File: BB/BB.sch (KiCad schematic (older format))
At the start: 37 parts, among them SW0 SW_Push, U1 AT90USB1286-AU, Y0 16Mhz

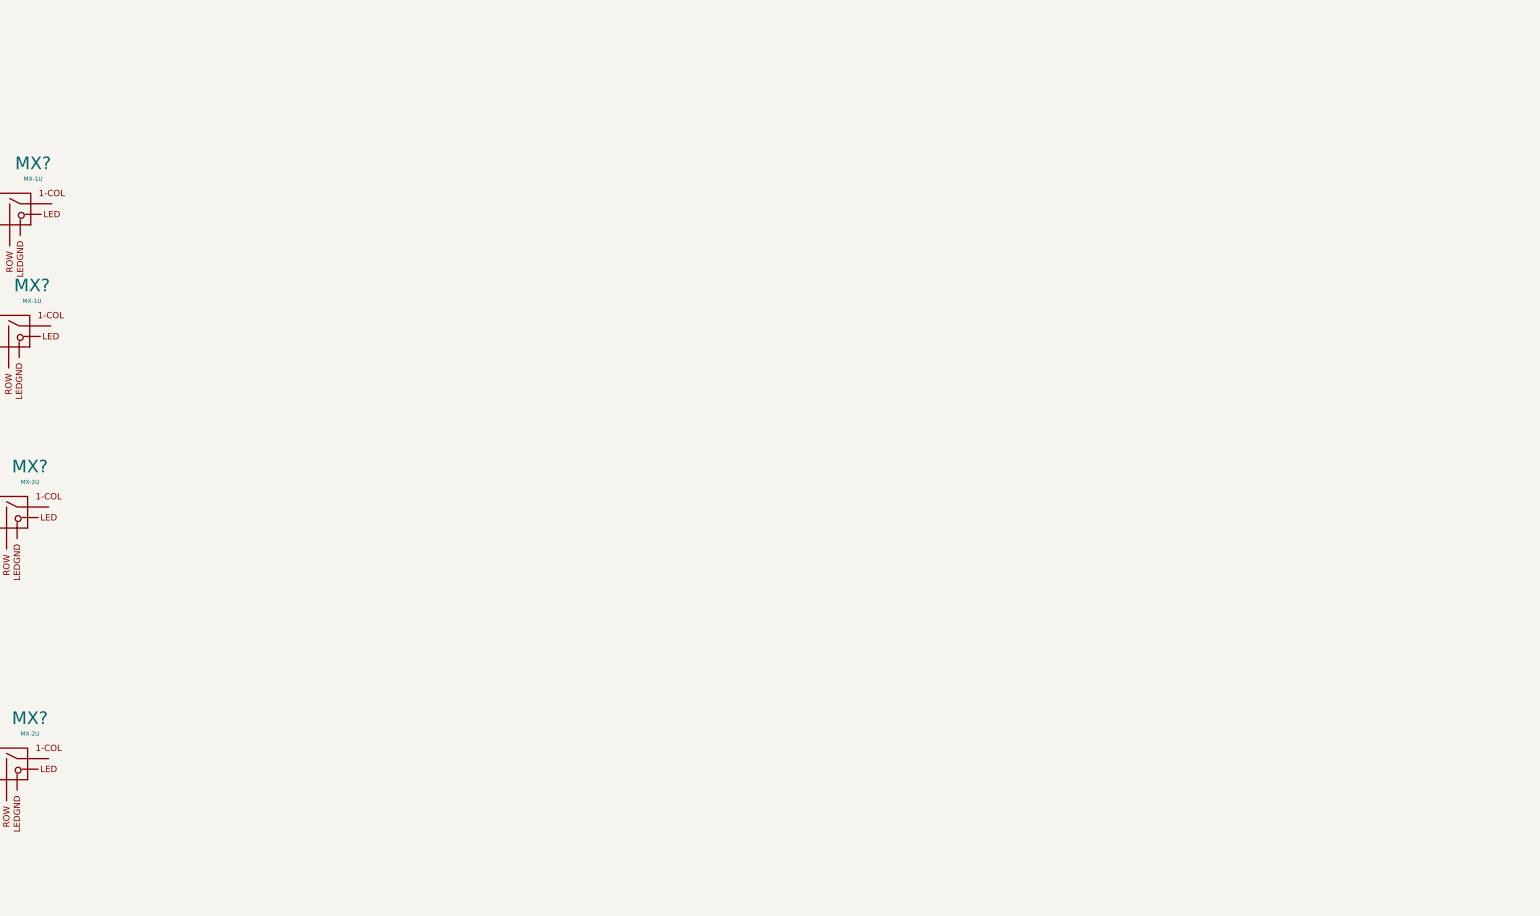
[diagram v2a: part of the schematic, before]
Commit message: All Switches In Place
No diodes yet, waiting for 2-1 diode schematic
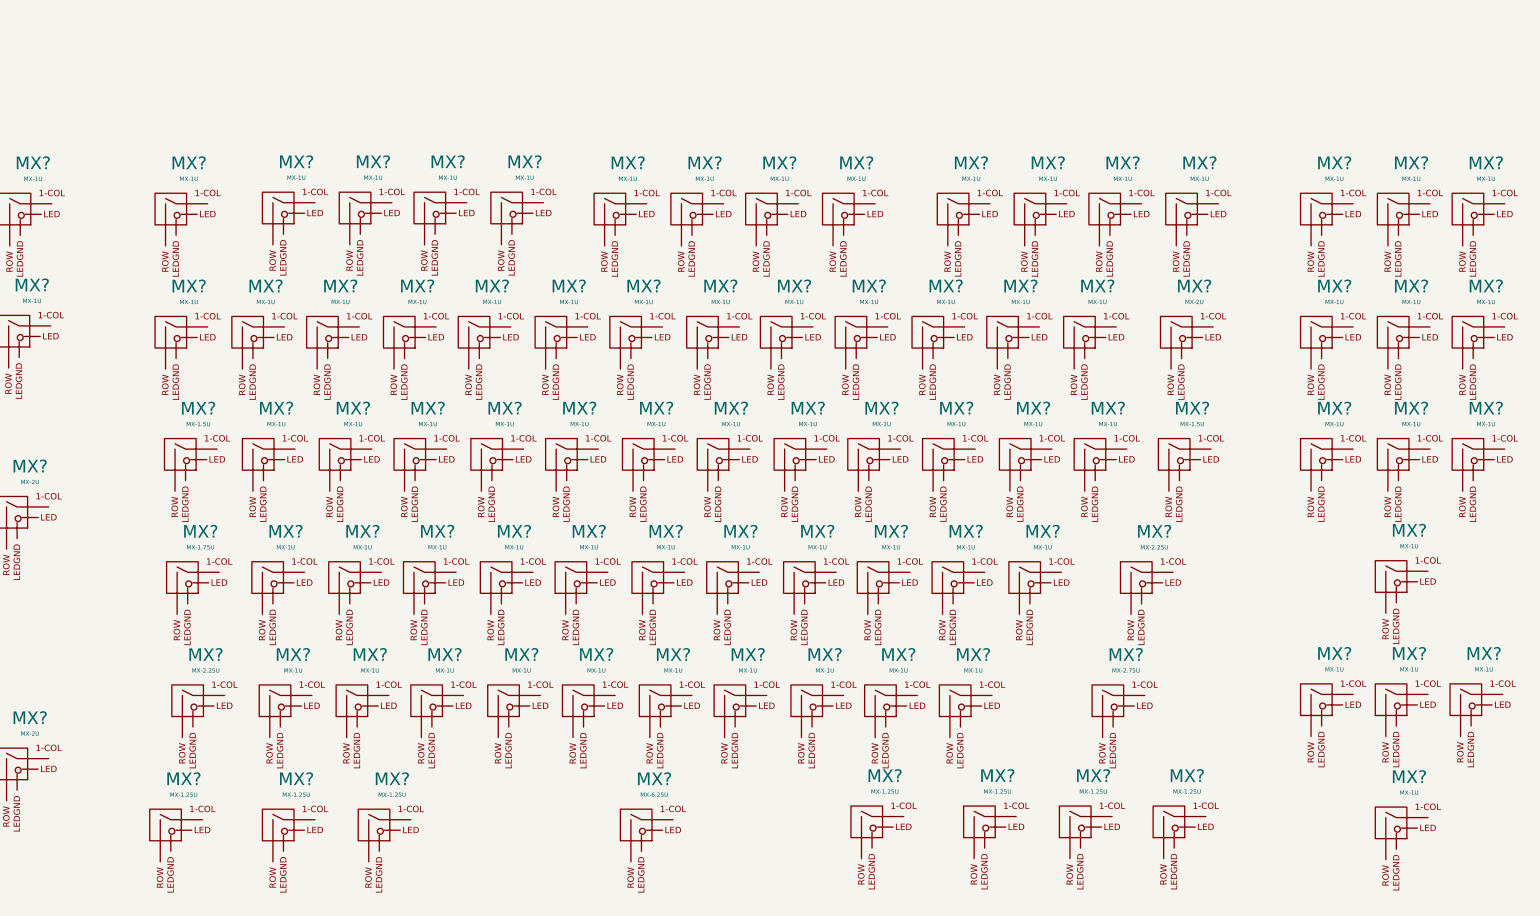
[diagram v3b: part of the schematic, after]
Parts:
- added MX? (x73): MX-1U, symbol MX_Alps_Hybrids:MX-1U
- added MX?: MX-2U, symbol MX_Alps_Hybrids:MX-2U
- added MX? (x2): MX-1.5U, symbol MX_Alps_Hybrids:MX-1.5U
- added MX? (x2): MX-2.25U, symbol MX_Alps_Hybrids:MX-2.25U
- added MX?: MX-1.75U, symbol MX_Alps_Hybrids:MX-1.75U
- added MX?: MX-2.75U, symbol MX_Alps_Hybrids:MX-2.75U
- added MX? (x7): MX-1.25U, symbol MX_Alps_Hybrids:MX-1.25U
- added MX?: MX-6.25U, symbol MX_Alps_Hybrids:MX-6.25U

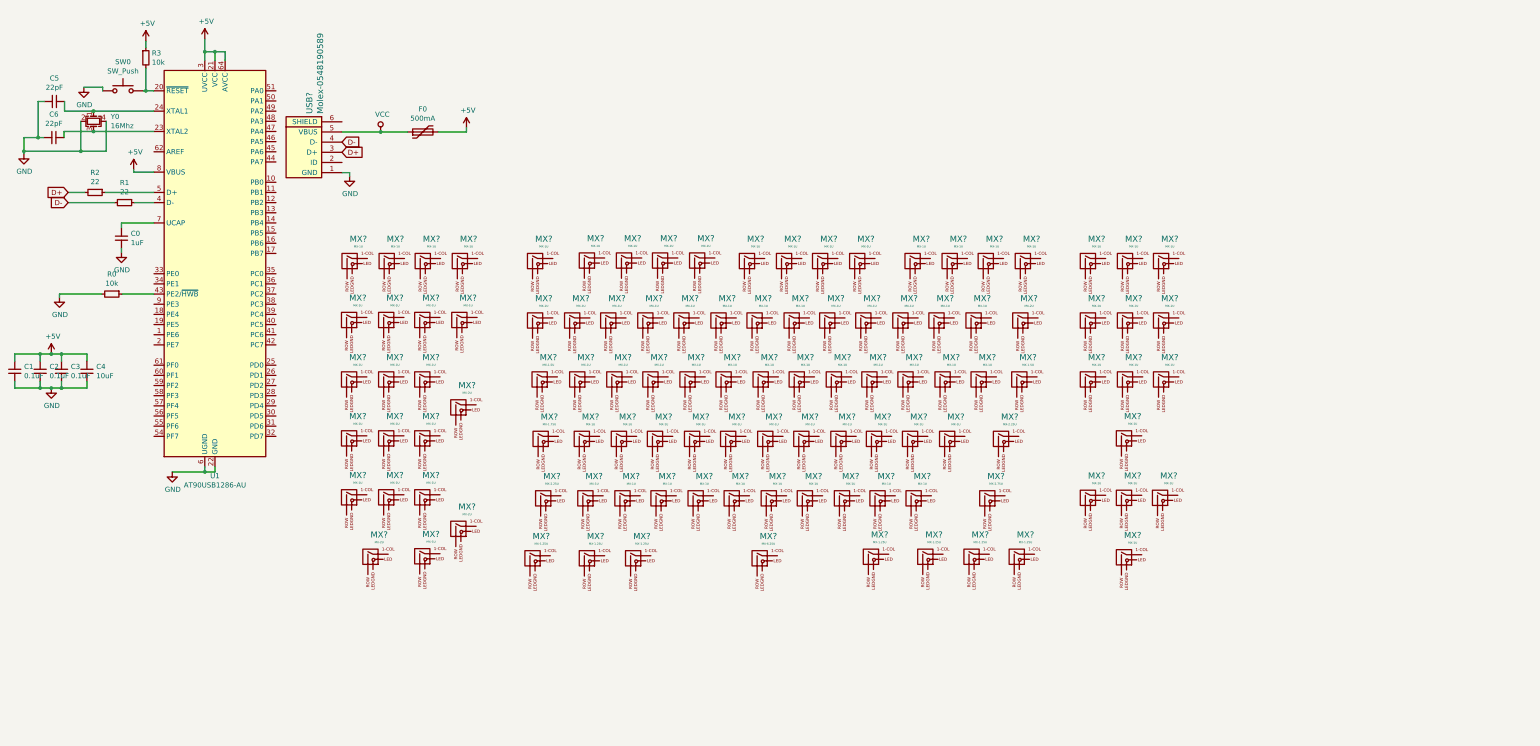
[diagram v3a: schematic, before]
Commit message: Add submodules
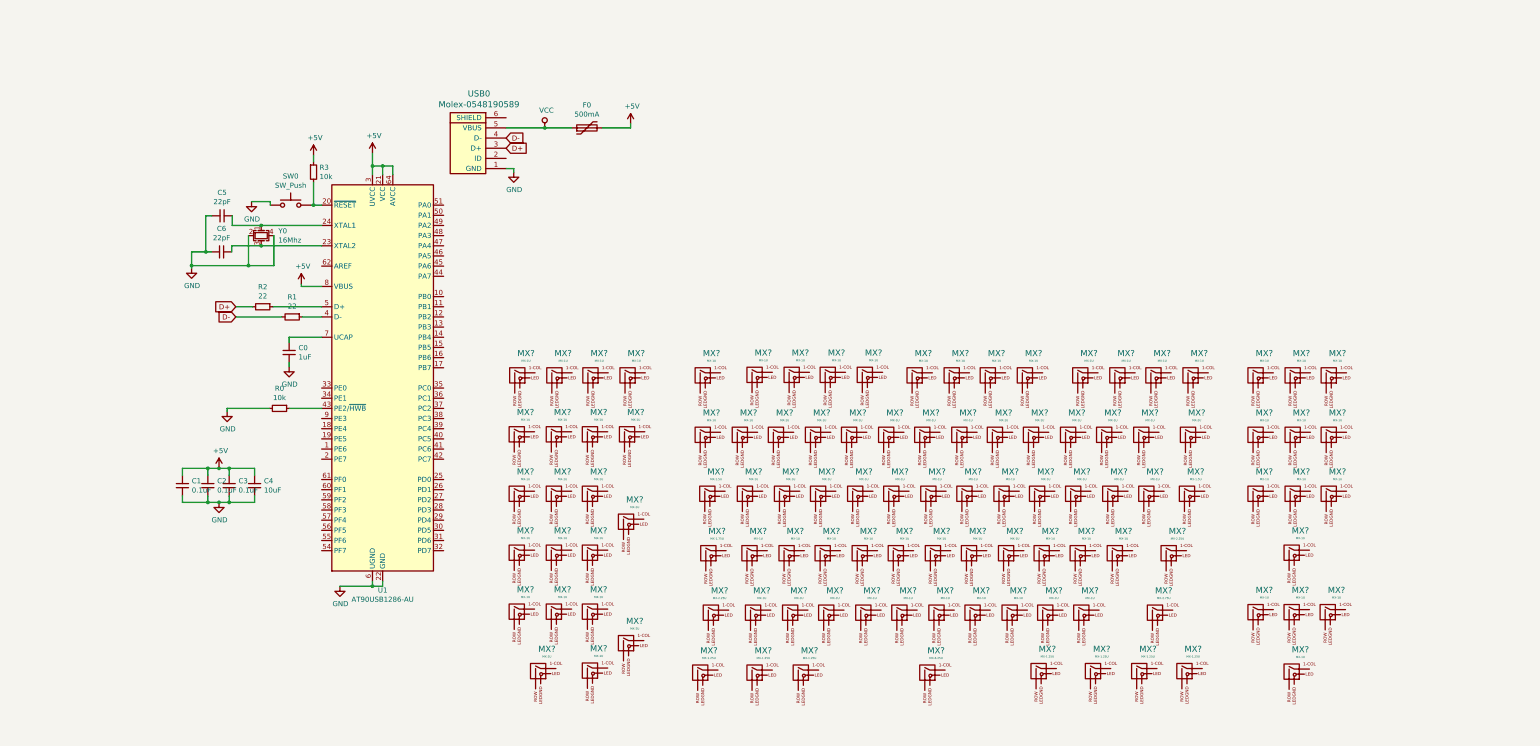
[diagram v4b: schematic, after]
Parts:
- gave numbers to parts that had none: 1
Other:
- moved on the sheet: C0, C1, C2, C3, C4, C5, C6, F0, MX?, R0, R1, R2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

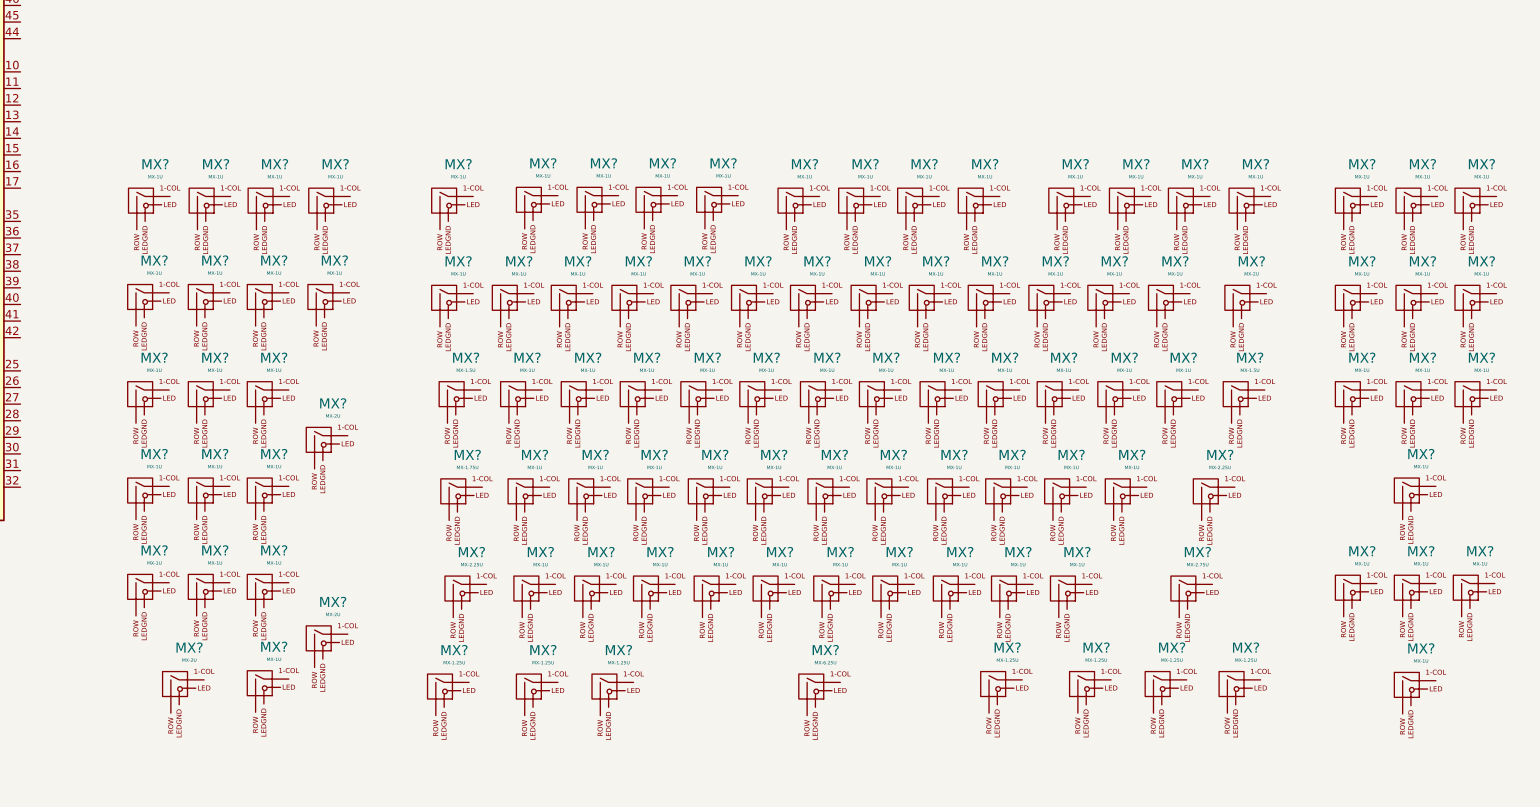
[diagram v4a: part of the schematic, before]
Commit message: All Switches in place with Diodes
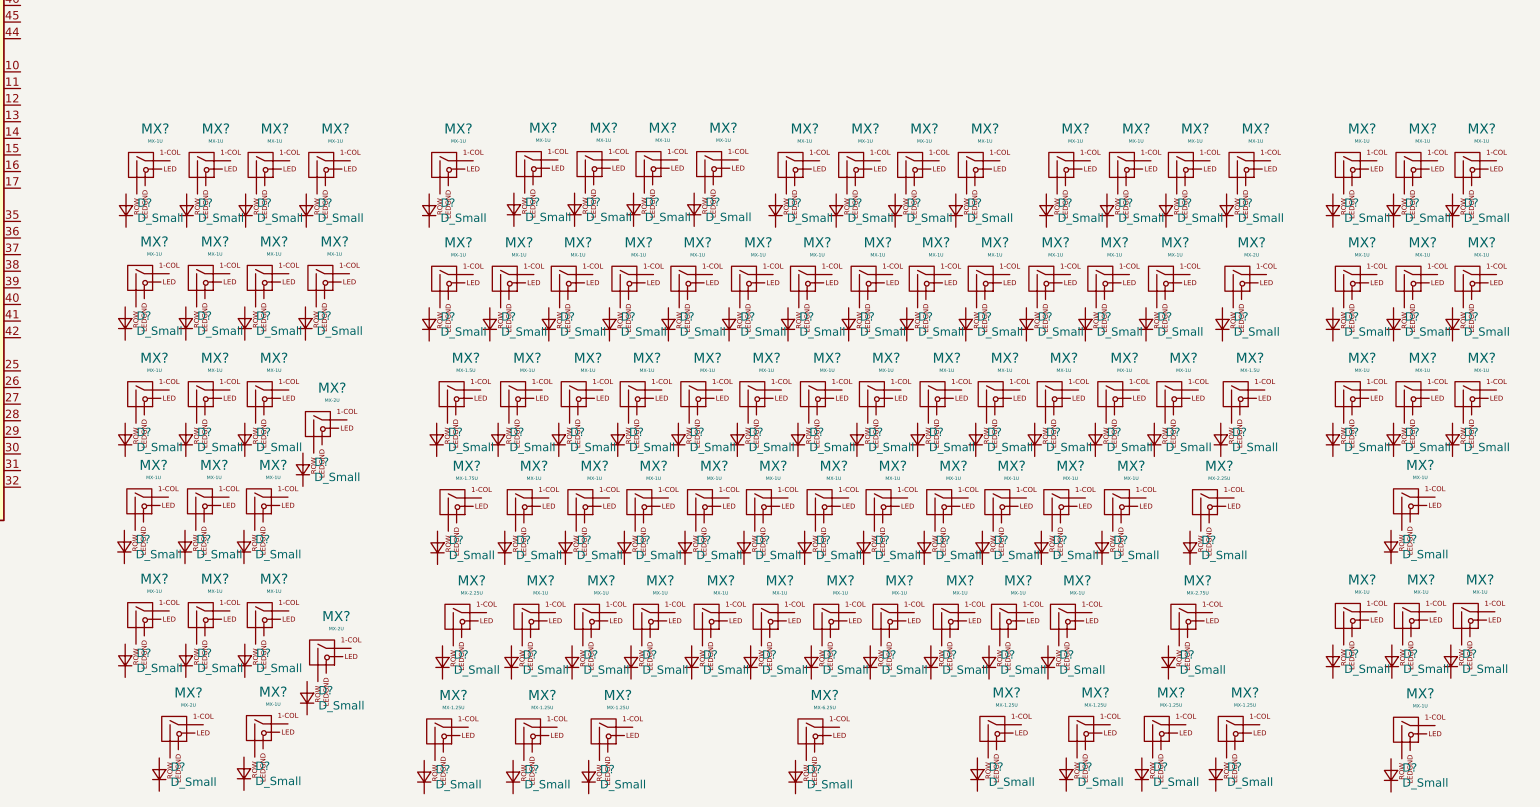
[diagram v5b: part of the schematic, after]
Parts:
- added D? (x109): D_Small, symbol Device:D_Small
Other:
- moved on the sheet: MX?
